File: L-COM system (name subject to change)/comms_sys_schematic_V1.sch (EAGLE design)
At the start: 48 parts, among them U1 TLV75733PDBVR, Y1 ECS-TXO-2016-33-120-TR

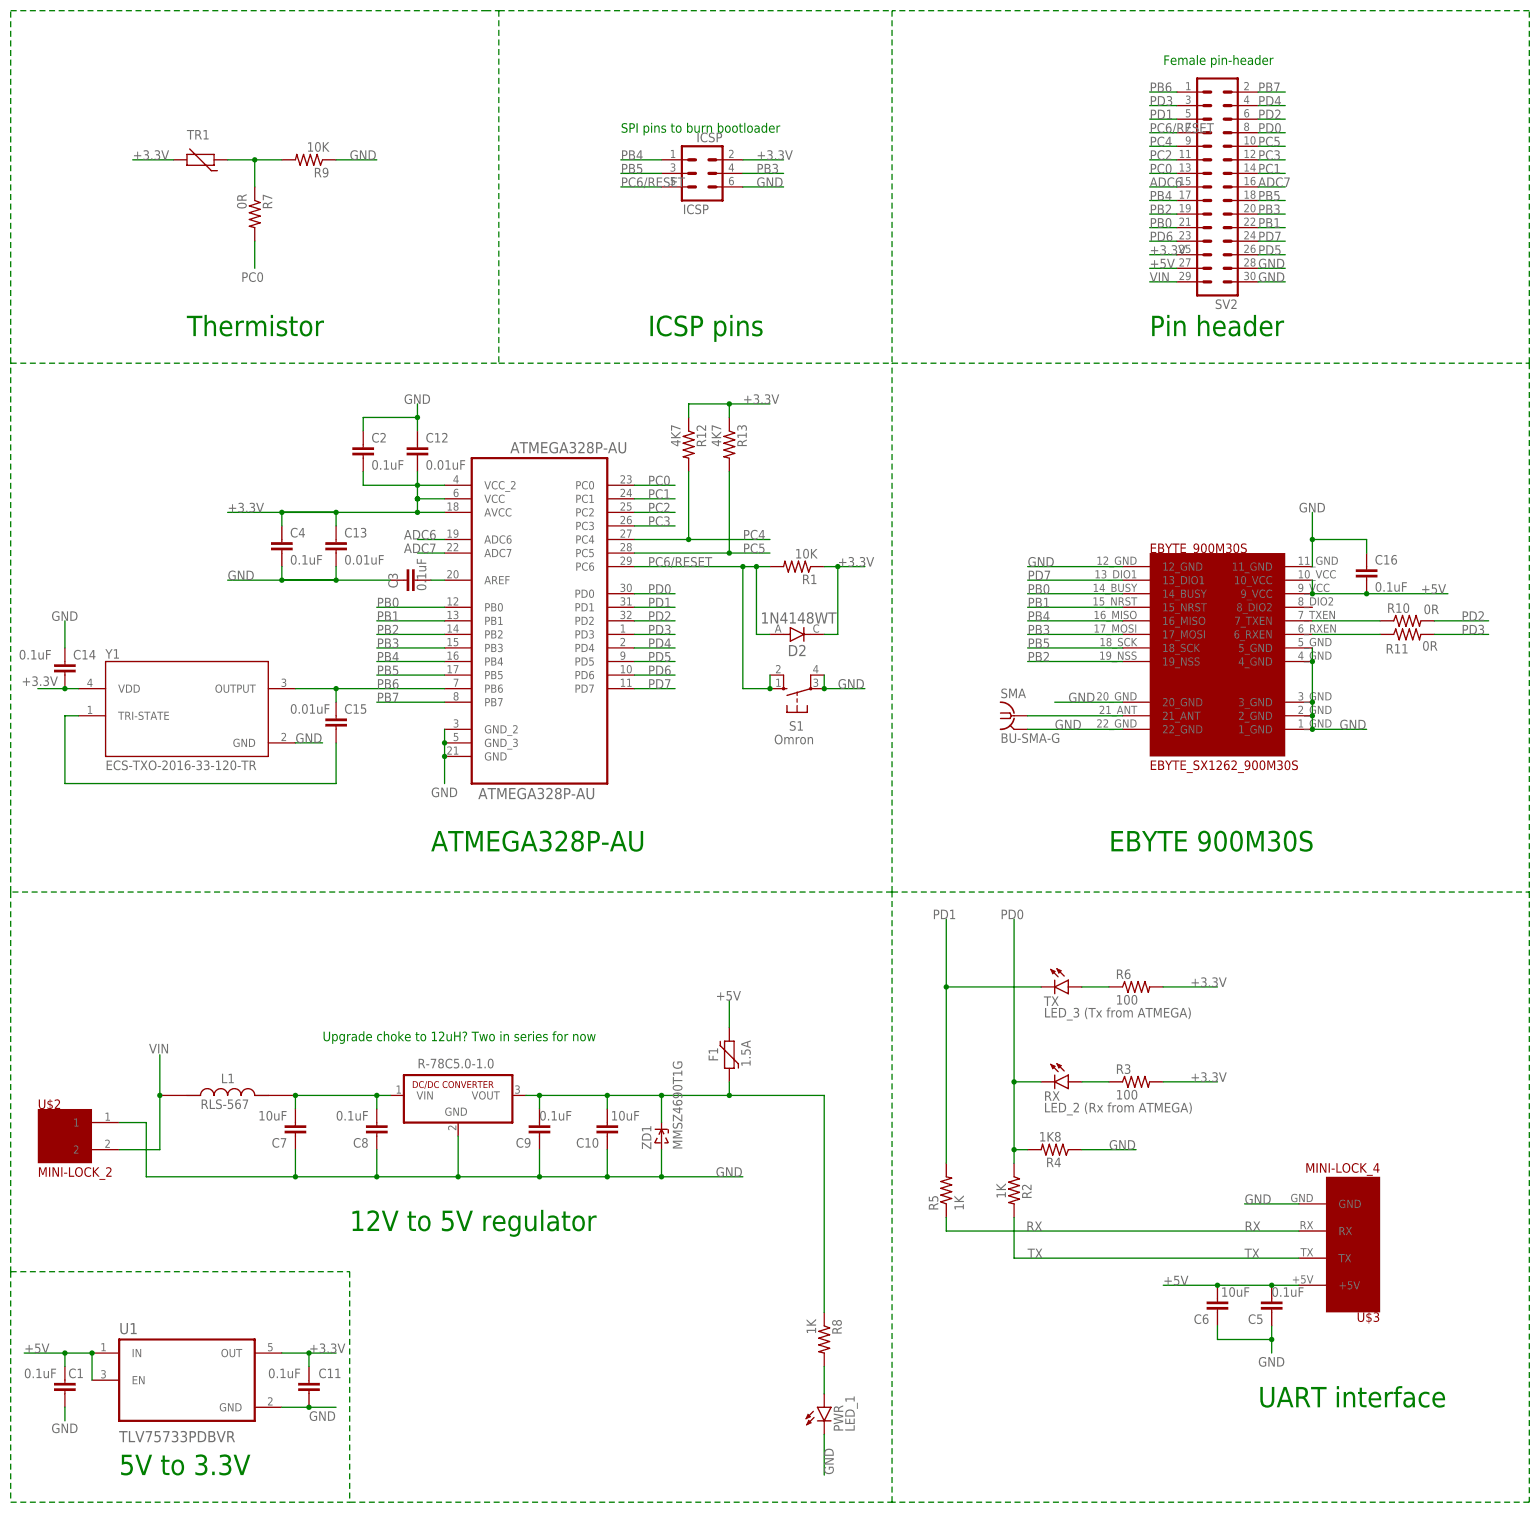
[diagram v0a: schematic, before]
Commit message: Various improvements/corrections
Posted on Reddit, applied reccomendations
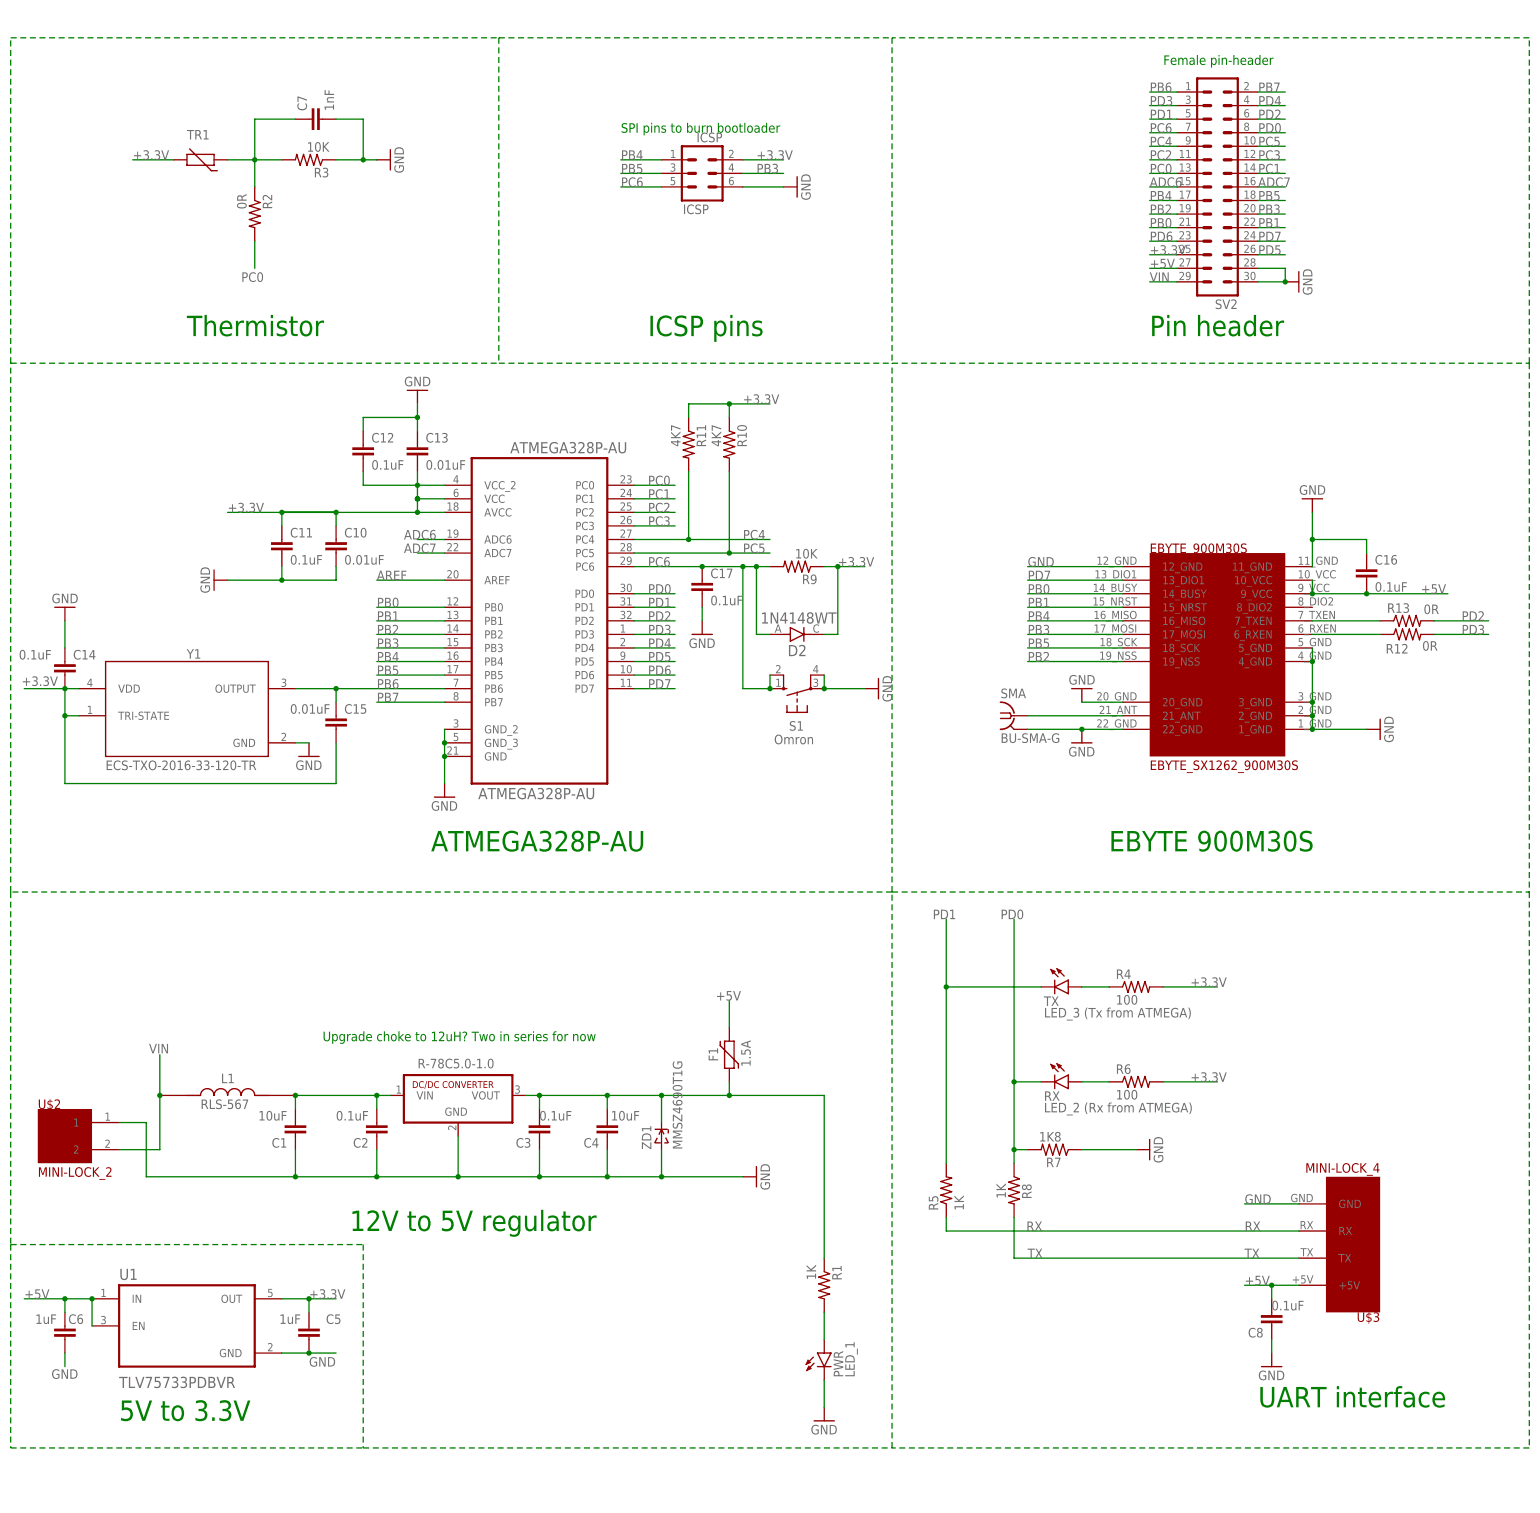
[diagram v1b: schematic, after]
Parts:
- removed C9: 0.1uF, rcl:C-EUC0805
- added C17: 0.1uF, rcl:C-EUC0805
- C1, C4: value 0.1uF -> 10uF
- C10: value 10uF -> 0.01uF
- C12: value 0.01uF -> 0.1uF
- C5: value 0.1uF -> 1uF
- C6: value 10uF -> 1uF
- C7: value 10uF -> 1nF
- R1: value 10K -> 1K
- R10, R11: value 0R -> 4K7
- R12, R13: value 4K7 -> 0R
- R2: value 1K -> 0R
- R3: value 100 -> 10K
- R4: value 1K8 -> 100
- R7: value 0R -> 1K8
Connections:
- removed net N$14: ATMEGA328P-AU.AREF, C3.2
- removed net N$5: C15.2, Y1.TRI-STATE
- removed net PC6/RESET: ATMEGA328P-AU.PC6, D2.A, ICSP.5, R1.2, S1.S, S1.S1, SV2.11
- new net AREF: ATMEGA328P-AU.AREF
- new net PC6: ATMEGA328P-AU.PC6, C17.1, D2.A, ICSP.5, R9.2, S1.S, S1.S1, SV2.11
- net $N77: now also C7.1, R2.1, R3.2; no longer R7.1, R9.2
- net +3.3V: now also C10.1, C11.1, C13.2, C15.2, C5.2, R10.1, R11.1, R4.2, R9.1, Y1.TRI-STATE; no longer C11.2, C13.1, C2.2, C4.1, R1.1, R12.1, R13.1, R3.2
- net +5V: now also C8.2; no longer C1.2, C5.2
- net GND: now also C10.2, C11.2, C13.1, C17.2, C4.1, C7.2, R3.1, R7.1; no longer C10.1, C11.1, C13.2, C4.2, C7.1, C9.1, R4.1, R9.1
- net N$1: now also C3.2, C4.2, R1.1; no longer C10.2, C9.2, R8.1
- net N$12: now also R6.1; no longer R3.1
- net N$16: now also R4.1; no longer R6.1
- net N$27: now also C1.2, C2.2; no longer C7.2, C8.2
- net N$4: now also R1.2; no longer R8.2
- net N$6: now also R13.1; no longer R10.1
- net N$7: now also R12.1; no longer R11.1
- net PC0: now also R2.2; no longer R7.2
- net PC4: now also R11.2; no longer R12.2
- net PC5: now also R10.2; no longer R13.2
- net PD0: now also R7.2, R8.1; no longer R2.1, R4.2
- net PD2: now also R13.2; no longer R10.2
- net PD3: now also R12.2; no longer R11.2
- net TX: now also R8.2; no longer R2.2
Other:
- moved on the sheet: C1, C10, C11, C12, C13, C2, C3, C4, C5, C6, C7, C8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

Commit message: Small fixes to board. Created parts list
Still need to source resistors, capacitors, fuses, etc.

Some of the components may be sourced from elsewhere for a lot cheaper, but this list keeps it all in Digikey.
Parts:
- removed R-78C5.0-1.0: R-78C5.0-1.0, dc-dc-converter:R-78C5.0-1.0
- removed SMA: BU-SMA-G, con-coax:BU-SMA-G
- added C9: 10V 22uF Tant, rcl:C-EUC1206
- added U2: TLV75733PDBVR, TLV75733PDBVR:TLV75733PDBVR
- added X1: SMA-142-0701-801/806, con-coax:SMA-142-0701-801/806
- C10, C13: value 0.01uF -> 10nF
- C11, C12, C16, C17, C2, C3, C8: value 0.1uF -> 100nF
- C14: value 0.1uF -> 10nF
- C15: value 0.01uF -> 10V 22uF Tant; device rcl:C-EUC0805 -> rcl:C-EUC1206
- EBYTE: value EBYTE_SX1262_900M30S -> EBYTE_900M30S
- LED_PWR: value LED_1 -> PWR
- LED_RX: value LED_2 (Rx from ATMEGA) -> RX
- LED_TX: value LED_3 (Tx from ATMEGA) -> TX
- R4, R6: value 100 -> 100R
- U1: value TLV75733PDBVR -> R-78C5.0-1.0; device TLV75733PDBVR:TLV75733PDBVR -> dc-dc-converter:R-78C5.0-1.0
- renumbered ATMEGA328P-AU to MCU1, D2 to D1, EBYTE_900M30S to EBYTE, PWR to LED_PWR, RX to LED_RX, SV2 to FH1, TX to LED_TX, U$2 to MX1, U$3 to MX2
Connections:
- net +3.3V: now also C9.1, U2.OUT; no longer C15.2, U1.OUT
- net +5V: now also C15.1, U2.EN, U2.IN; no longer U1.EN, U1.IN
- net GND: now also C15.2, C9.2, U2.GND, X1.2; no longer R-78C5.0-1.0.GND, SMA.2
- net N$1: now also U1.VOUT; no longer R-78C5.0-1.0.VOUT
- net N$27: now also U1.VIN; no longer R-78C5.0-1.0.VIN
- net N$8: now also X1.1; no longer SMA.1
- net PB6: no longer C15.1
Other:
- moved on the sheet: C15

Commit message: V1 design finished, full parts list
First version finished, complete parts list put together.

Boards currently ordered from PCBWay to try out the design.
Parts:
- removed S1: Omron, switch-omron:10-XX
- removed TR1: (no value), discrete:THERMISTOR_R-2,5
- added R14: 0R, rcl:R-US_R0805
- added SW1: (no value), Wurth_Elektronik_Electromechanic_Switch_rev16c:430152043826
- C15, C9: value 10V 22uF Tant -> 10V 33uF Tant
- F1: value 1.5A -> 1A
- R10: value 4K7 -> 10K
- R12: value 0R -> 4K7
- R4: value 100R -> 1624345-1; device rcl:R-US_R0805 -> 1624345-1:1624345-1
- R5: value 1K -> 200R
- R6: value 100R -> 1K
- R7: value 1K8 -> 200R
- R8: value 1K -> 1K8
- R9: value 10K -> 1K
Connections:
- net $N77: now also R4.2; no longer TR1.1
- net +3.3V: now also R12.1, R4.1, R5.2, R7.2; no longer R4.2, R6.2, R9.1, TR1.2
- net GND: now also R8.1, SW1.2, SW1.4; no longer R7.1, S1.P, S1.P1
- net N$12: now also R7.1; no longer R6.1
- net N$16: now also R5.1; no longer R4.1
- net N$6: now also R14.1; no longer R13.1
- net N$7: now also R13.1; no longer R12.1
- net PC4: now also R12.2; no longer R11.2
- net PC5: now also R11.2; no longer R10.2
- net PC6: now also R10.2, SW1.1, SW1.3; no longer R9.2, S1.S, S1.S1
- net PD0: now also R8.2, R9.1; no longer R7.2, R8.1
- net PD1: now also R6.2; no longer R5.2
- net PD2: now also R14.2; no longer R13.2
- net PD3: now also R13.2; no longer R12.2
- net RX: now also R6.1; no longer R5.1
- net TX: now also R9.2; no longer R8.2
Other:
- moved on the sheet: R10, R11, R12, R13, R5, R6, R7, R8, R9
